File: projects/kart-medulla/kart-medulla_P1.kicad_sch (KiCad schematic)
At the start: 55 parts, among them CN1 1990012, CN10 1990012, CN2 1990012, CN3 1990012, CN4 1990012, CN5 1990012, CN6 1990012, CN7 1990012, CN8 1990012, CN9 1990012, Q3 IRLZ44NPBF, Q4 BSS123_C5184436, U13 MCP4922-E/SL, U14 MAX4660EUA+T, U19 L7805CDT_C20611927, U23 SSW-122-01-T-D, U24 SSW-122-01-T-S, U25 PCF8574T/3,518, U4 LM358DR, U5 SN74LVC3G17DCTR

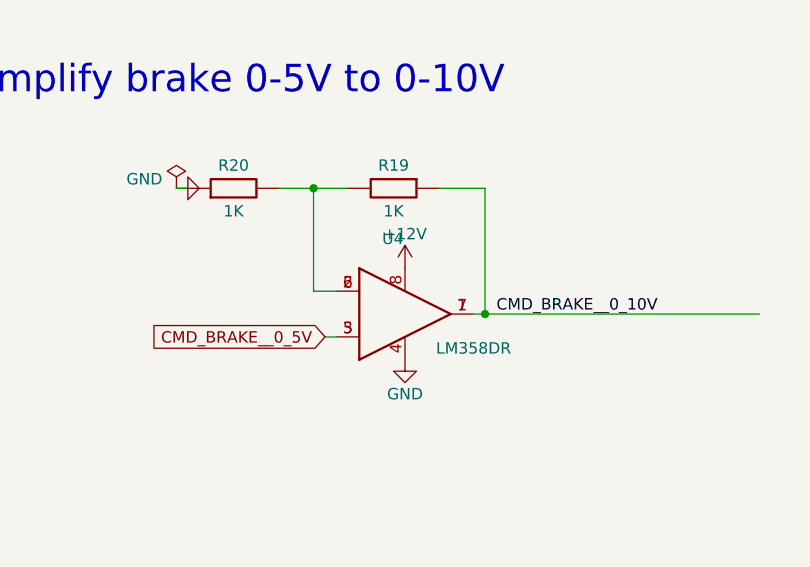
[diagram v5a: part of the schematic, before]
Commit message: kart-medulla: split LM358DR into proper multi-unit symbol (op-amp A + B)
ConvertEDA collapsed both op-amps onto one unit with pins 5/6/7
geometrically stacked on top of pins 3/2/1, causing pin_to_pin
errors (OUT1 + OUT2 short). Restructured into KiCad multi-unit
form: unit 1 keeps pins 1,2,3,4,8 at original lib coords (existing
U4 wiring preserved untouched); unit 2 contains pins 5,6,7 only.
Applied to both the project lib and the schematic lib_symbols
cache. ERC: 60 → 61 (0 errors / 61 warnings). The new
missing_unit / missing_input_pin warnings are expected — unit B
is now a separate placeable unit; place it with tie-back wiring
(IN+ → GND, IN- → OUT) to silence them and document the safe
state of the unused op-amp half.

Co-Authored-By: Claude Opus 4.7 (1M context) <noreply@anthropic.com>
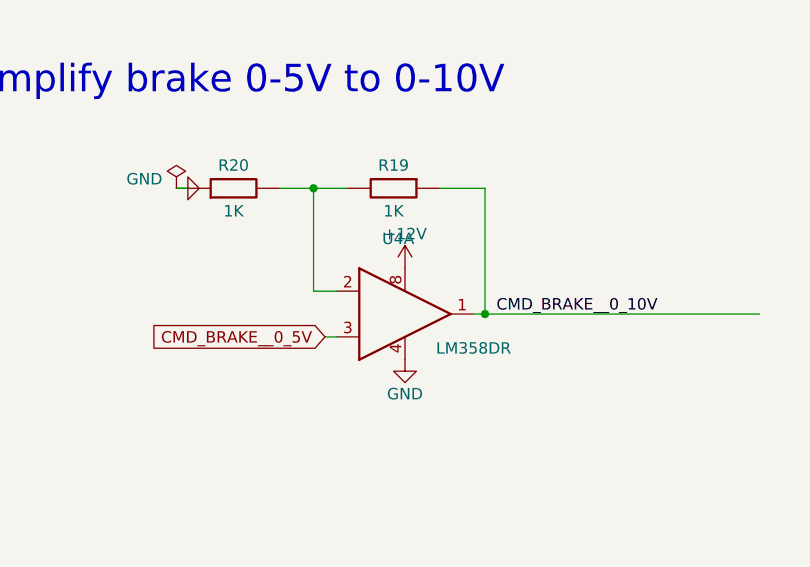
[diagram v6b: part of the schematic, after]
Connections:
- net CMD_BRAKE__0_10V: no longer U4.7 (OUT2)
- net CMD_BRAKE__0_5V: no longer U4.5 (+IN2)
- net at R19.2, R20.2, U4.2 (-IN1): no longer U4.6 (-IN2)

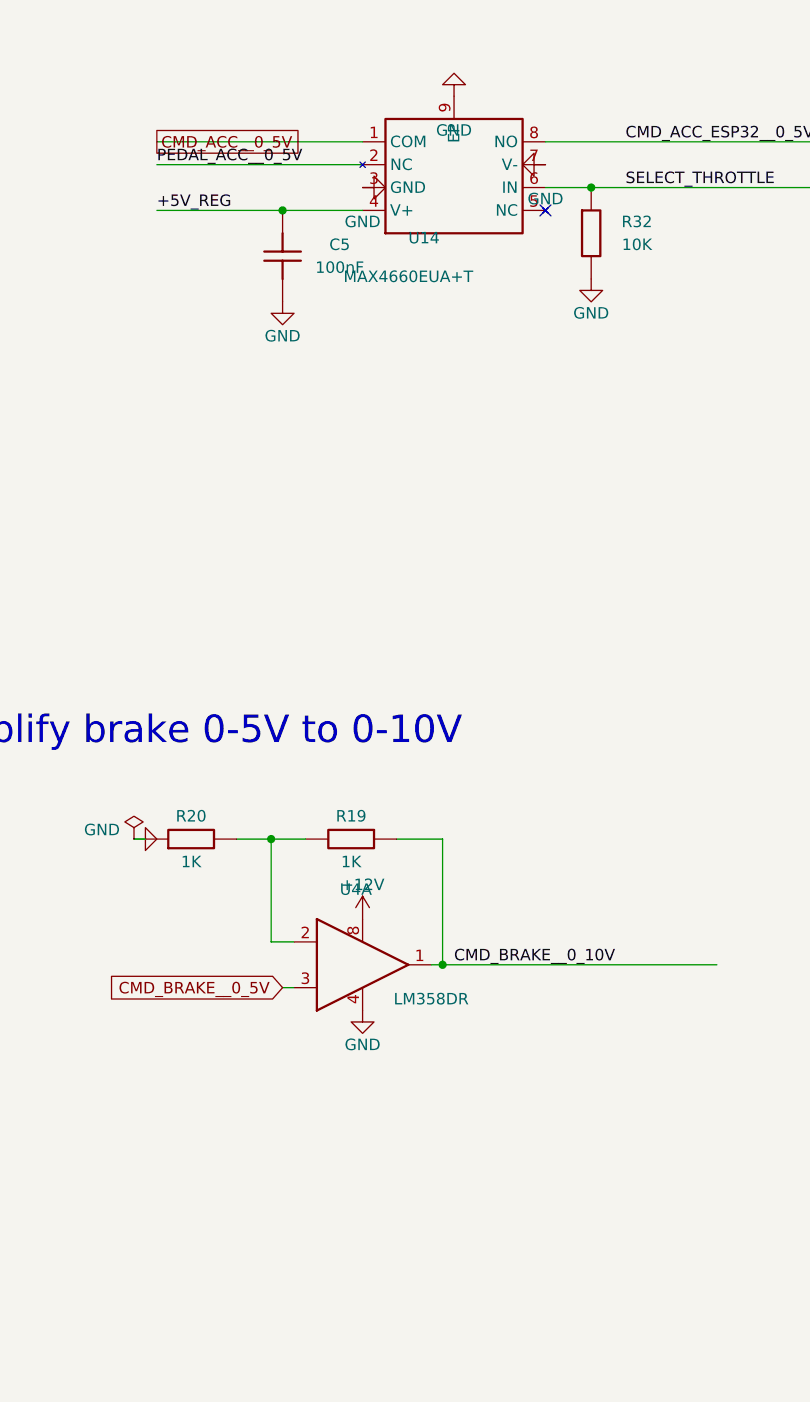
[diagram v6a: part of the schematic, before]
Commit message: kart-medulla: NC markers on op-amp B + fix MAX4660 pin 2 etype
Two cleanups:
1. Place 3 (no_connect) markers on U1B (LM358 op-amp B) pins 5/6/7
   to silence missing_unit + missing_input_pin warnings.
2. Fix MAX4660 pin 2 electrical type from no_connect to passive.
   The MAX4660 is a SPDT analog switch with two pins both named
   'NC' in the symbol but with different meanings: pin 2 is the
   *Normally Closed* switch contact (real functional pin, wired
   to PEDAL_ACC__0_5V), pin 5 is genuine *No Connect* (no internal
   silicon). I had set both to no_connect, which fired
   no_connect_connected on pin 2.

ERC: 61 → 58, 0 errors, 58 warnings (47 wire-endpoint + 11 isolated
single-pin labels — all legitimate or GUI-only cleanup).

Co-Authored-By: Claude Opus 4.7 (1M context) <noreply@anthropic.com>
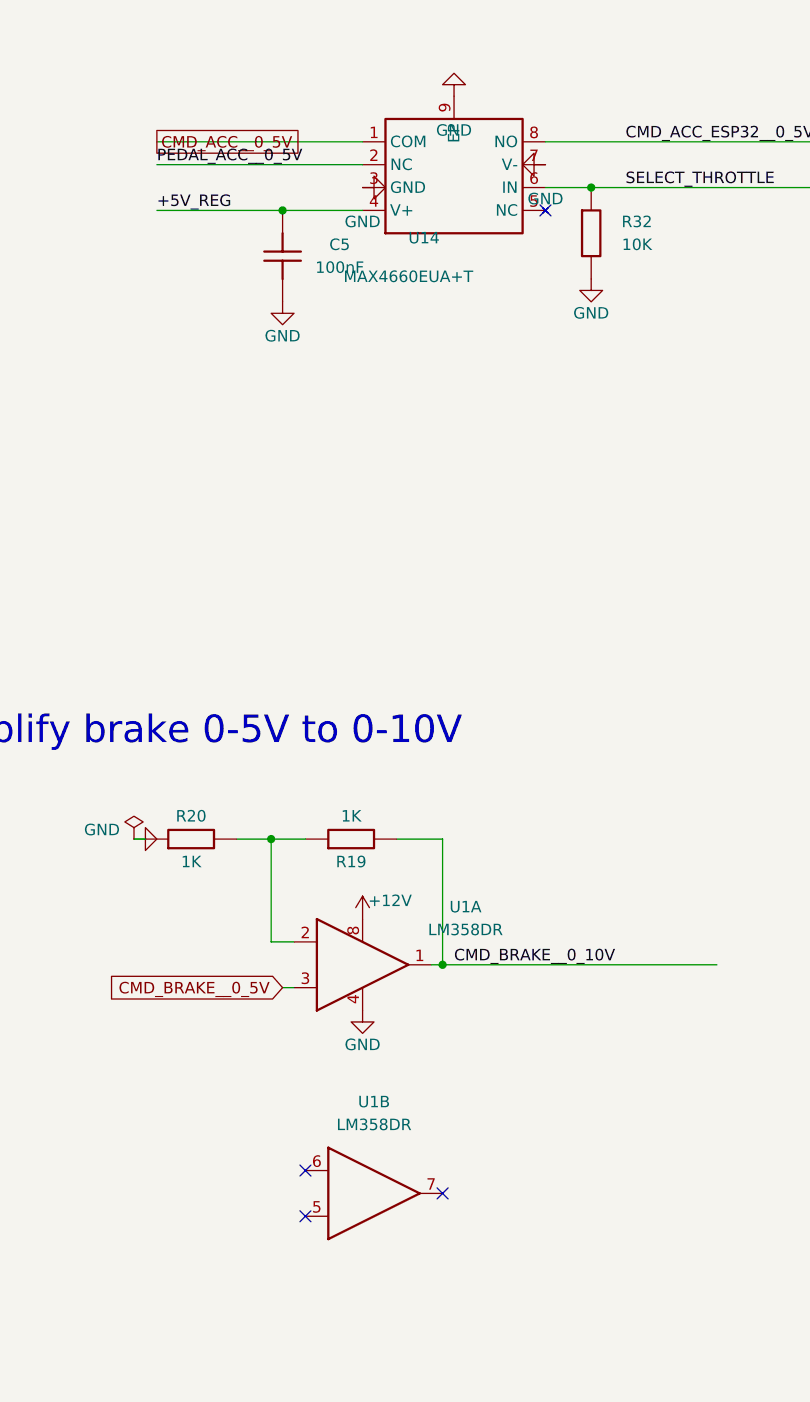
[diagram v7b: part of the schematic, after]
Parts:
- removed U4: LM358DR, kart-medulla:SOIC-8_L5.0-W4.0-P1.27-LS6.0-BL, symbol kart-medulla:LM358DR
- added U1: LM358DR, symbol kart-medulla:LM358DR
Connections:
- net +12V: now also U1.8 (+V)
- net CMD_BRAKE__0_10V: now also R19.2, U1.1 (OUT1); no longer R19.1
- net CMD_BRAKE__0_5V: now also U1.3 (+IN1)
- net GND: now also U1.4 (GND)
- net at R20.2: now also R19.1, U1.2 (-IN1); no longer R19.2
- no-connect marks 10 -> 13
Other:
- moved on the sheet: R19
